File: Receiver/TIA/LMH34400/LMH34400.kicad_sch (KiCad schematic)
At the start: 24 parts, among them J1 TEST, J2 Conn_Coaxial, J3 Vout, J4 N_EN, J5 N_ALC, J6 Conn_Coaxial, U1 XLMH34400IDRLR

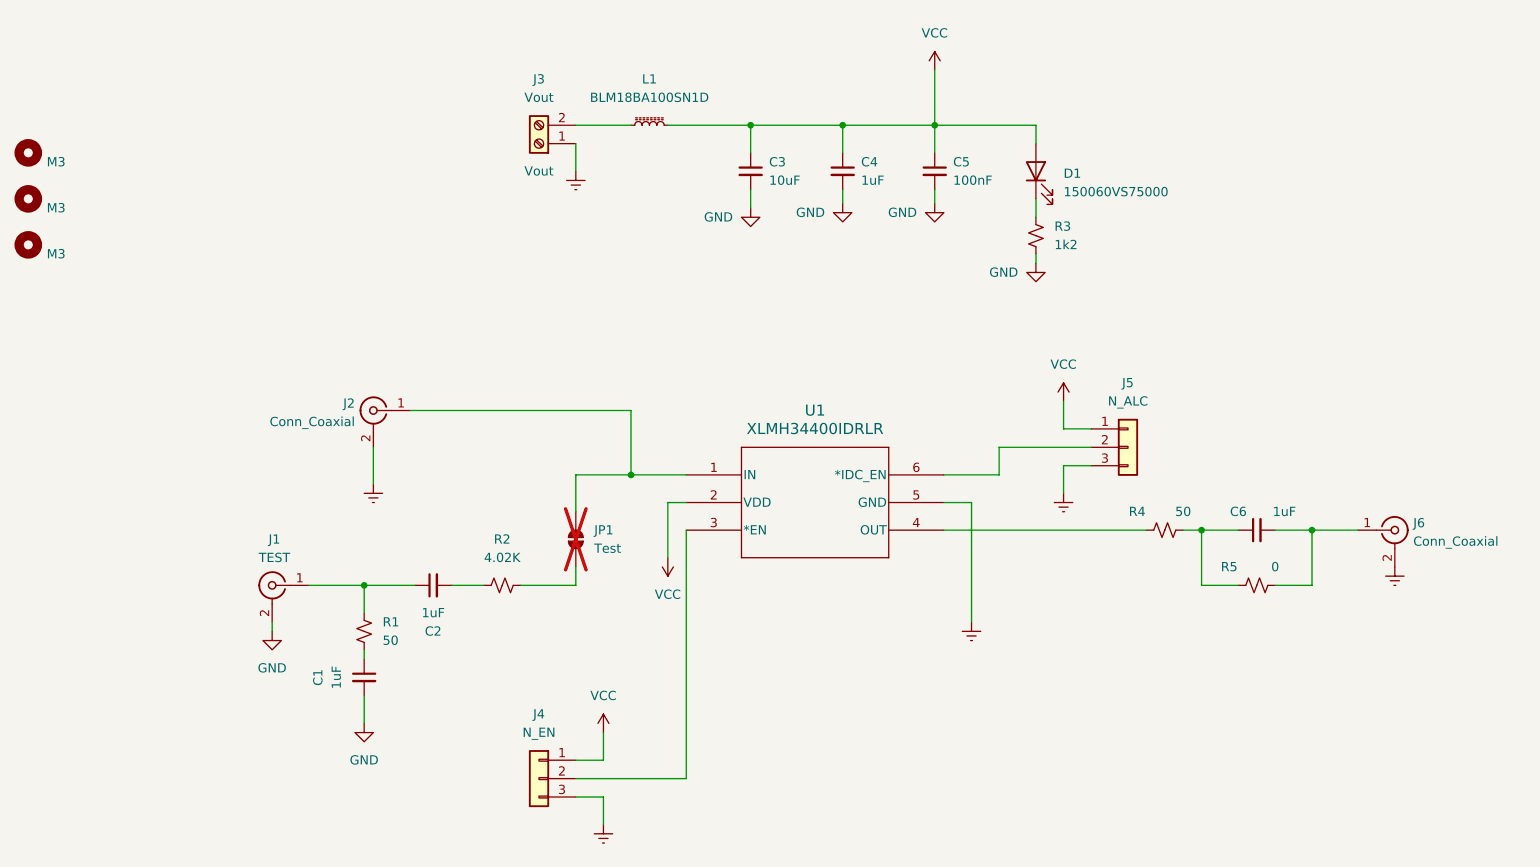
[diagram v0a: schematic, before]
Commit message: LMH34400 first versio
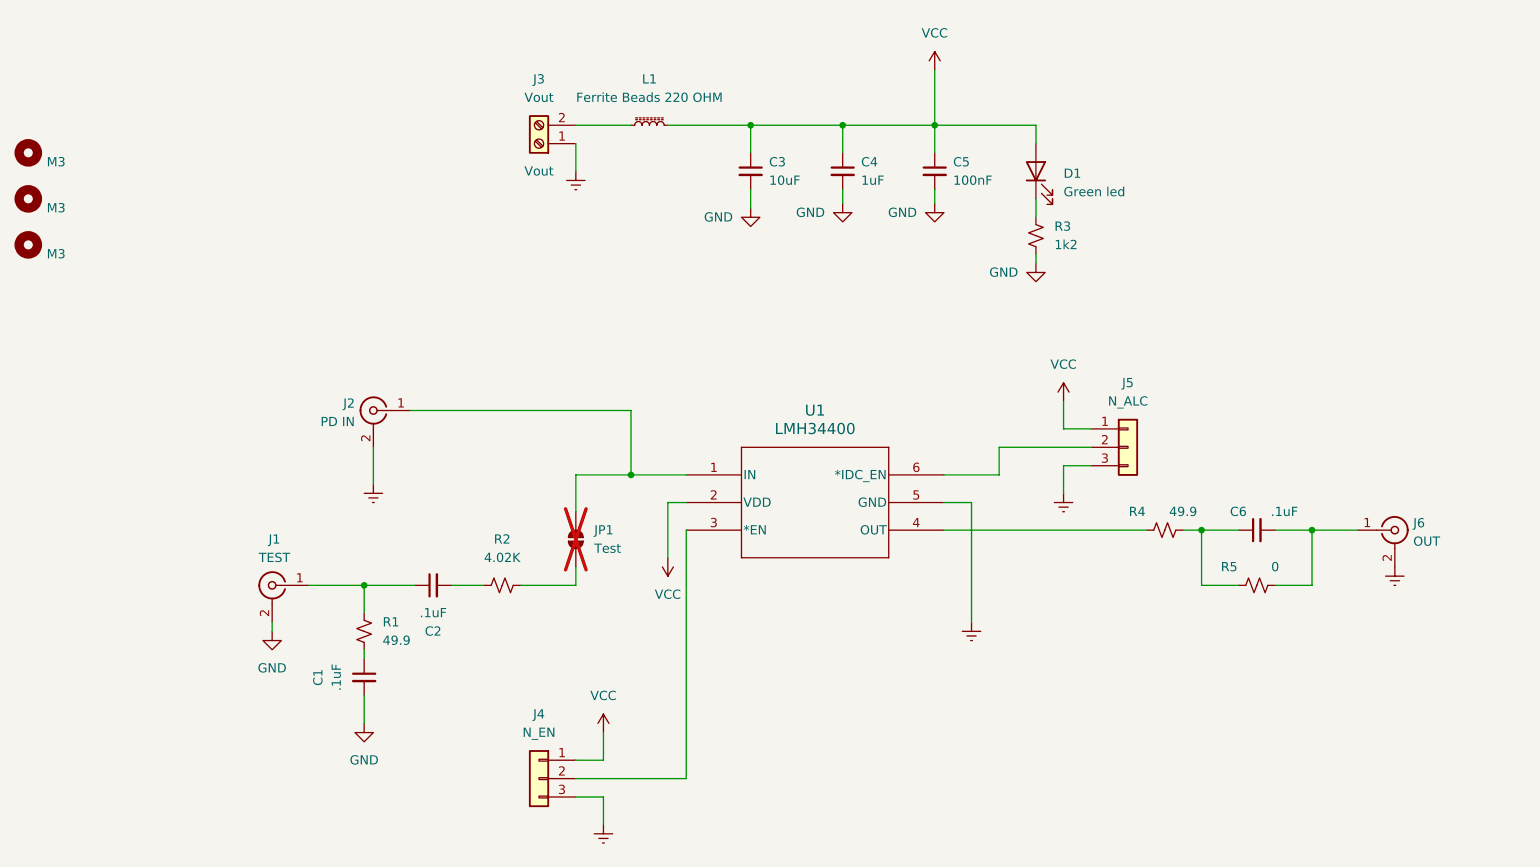
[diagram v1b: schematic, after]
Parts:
- C1, C2, C6: value 1uF -> .1uF; footprint Capacitor_SMD:C_0603_1608Metric_Pad1.08x0.95mm_HandSolder -> Capacitor_SMD:C_0402_1005Metric_Pad0.74x0.62mm_HandSolder; Manufacturer (none) -> KYOCERA AVX; Manufacturer Part Number (none) -> 530L104KT16; Mouser Part Number (none) -> 581-530L104KT16
- C3: Manufacturer (none) -> Murata Electronics; Manufacturer Part Number (none) -> GRM188Z71A106MA73D; Mouser Part Number (none) -> 81-GRM188Z71A106MA3D
- C4: Manufacturer (none) -> Samsung Electro-Mechanics; Manufacturer Part Number (none) -> CL10B105KP8NNNC; Mouser Part Number (none) -> 187-CL10B105KP8NNNC
- C5: Manufacturer (none) -> Samsung Electro-Mechanics; Manufacturer Part Number (none) -> CL10B104KO8NFNC; Mouser Part Number (none) -> 187-CL10B104KO8NFNC
- D1: value 150060VS75000 -> Green led; Manufacturer (none) -> Wurth Elektronik; Manufacturer Part Number (none) -> 150060VS75000; Mouser Part Number (none) -> 710-150060VS75000
- J2: value Conn_Coaxial -> PD IN
- J6: value Conn_Coaxial -> OUT
- JP1: Manufacturer (none) -> Vishay / Beyschlag; Manufacturer Part Number (none) -> MCT0603MZ0000ZP500; Mouser Part Number (none) -> 594-MCT0603MZ0000ZP5; now in the parts list
- L1: value BLM18BA100SN1D -> Ferrite Beads 220 OHM; Manufacturer (none) -> Murata Electronics; Manufacturer Part Number (none) -> BLM18KG221SN1D; Mouser Part Number (none) -> 81-BLM18KG221SN1D
- R1, R4: value 50 -> 49.9; Manufacturer (none) -> Vishay / Beyschlag; Manufacturer Part Number (none) -> MCT06030C4999FP500; Mouser Part Number (none) -> 594-MCT06030C4999FP5
- R2: Manufacturer (none) -> Vishay / Beyschlag; Manufacturer Part Number (none) -> MCT06030C4021FP500; Mouser Part Number (none) -> 594-MCT06030C4021FP5
- R3: Manufacturer (none) -> Vishay / Dale; Manufacturer Part Number (none) -> CRCW08051K20FKEAC; Mouser Part Number (none) -> 71-CRCW08051K20FKEAC
- R5: Manufacturer (none) -> Vishay / Beyschlag; Manufacturer Part Number (none) -> MCT0603MZ0000ZP500; Mouser Part Number (none) -> 594-MCT0603MZ0000ZP5
- U1: value XLMH34400IDRLR -> LMH34400; Manufacturer (none) -> Texas Instruments; Manufacturer Part Number (none) -> LMH34400IDRLR; Mouser Part Number (none) -> 595-LMH34400IDRLR

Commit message: LTC6268-10 first version
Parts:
- D1: footprint LumiCom_TIA:LEDC1608X80N -> LED_SMD:LED_0603_1608Metric
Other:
- moved on the sheet: C1, C2, C3, C4, C5, C6, D1, J1, J2, J3, J4, J5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

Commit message: LMH3440 fixed
LMH3440 fixed
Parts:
- R3: Manufacturer Part Number CRCW08051K20FKEAC -> CRCW06031K20FKEA; Mouser Part Number 71-CRCW08051K20FKEAC -> 71-CRCW0603-1.2K-E3
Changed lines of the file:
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@@
 			)
 		)
-		(property "Datasheet" "https://www.vishay.com/doc?28773"
+		(property "Datasheet" "https://www.vishay.com/doc?20035"
 			(at 195.58 68.58 0)
 			(effects
@@
 			)
 		)
-		(property "Description" "1/8Watt 1.2Kohms 1% Commercial Use"
+		(property "Description" " Thick Film Resistors - SMD 1/10watt 1.2Kohms 1% 0603"
 			(at 195.58 68.58 0)
 			(effects
@@
 			)
 		)
-		(property "Manufacturer Part Number" "CRCW08051K20FKEAC"
+		(property "Manufacturer Part Number" " CRCW06031K20FKEA "
 			(at 195.58 68.58 0)
 			(effects
@@
 			)
 		)
-		(property "Mouser Part Number" " 71-CRCW08051K20FKEAC "
+		(property "Mouser Part Number" " 71-CRCW0603-1.2K-E3 "
 			(at 195.58 68.58 0)
 			(effects

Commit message: Rx Amp first version
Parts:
- JP1: now fitted
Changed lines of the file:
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@@
 		(in_bom yes)
 		(on_board yes)
-		(dnp yes)
+		(dnp no)
 		(fields_autoplaced yes)
 		(property "Reference" "JP1"
